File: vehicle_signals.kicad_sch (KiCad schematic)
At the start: 24 parts, among them IC4 TLIN1027DRQ1, U10 LTV-827S, U11 LTV-827S, U12 LTV-827S, U13 LTV-827S

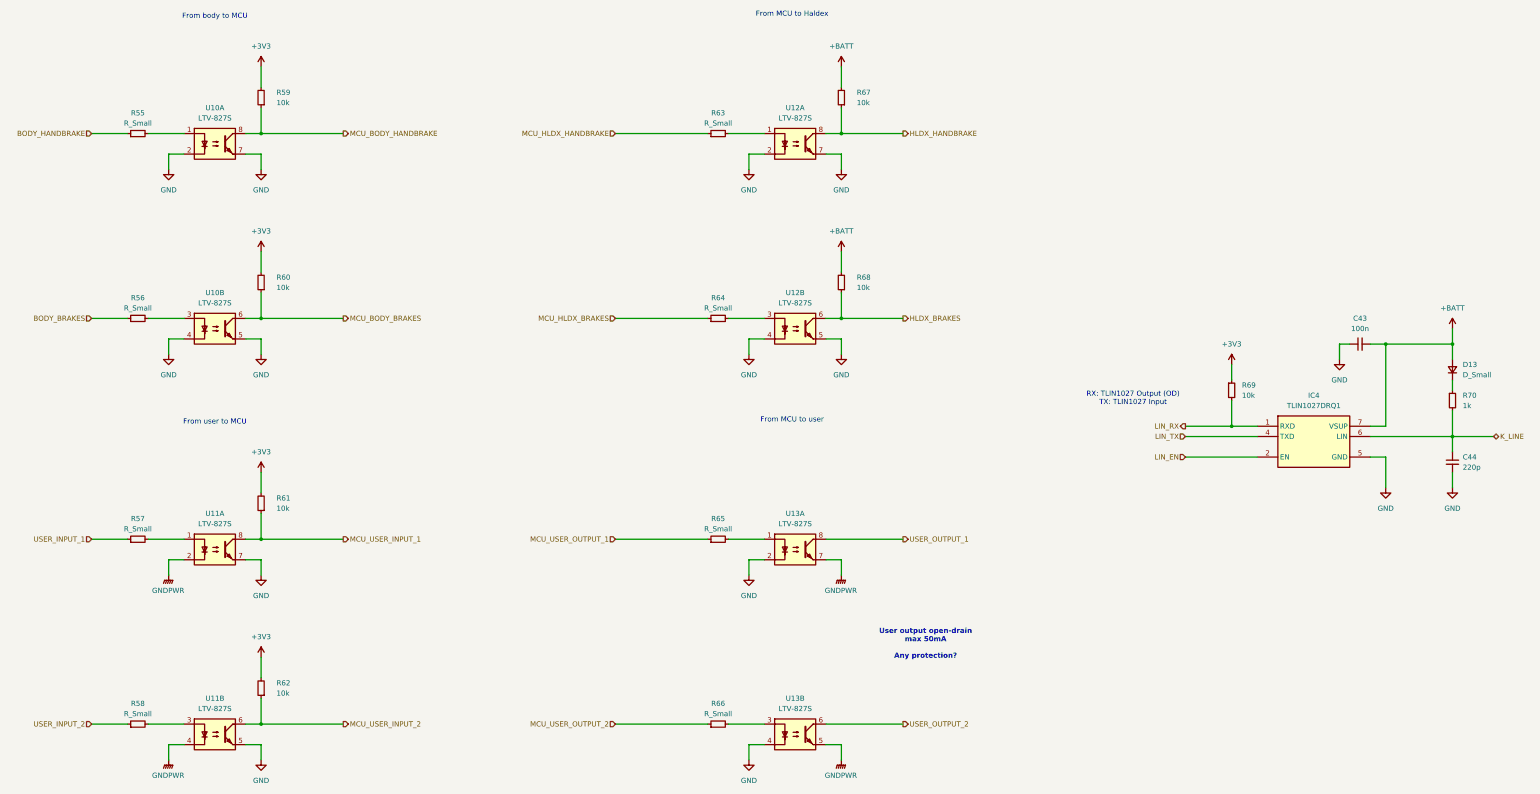
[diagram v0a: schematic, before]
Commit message: vehicle signals: using solid state relais
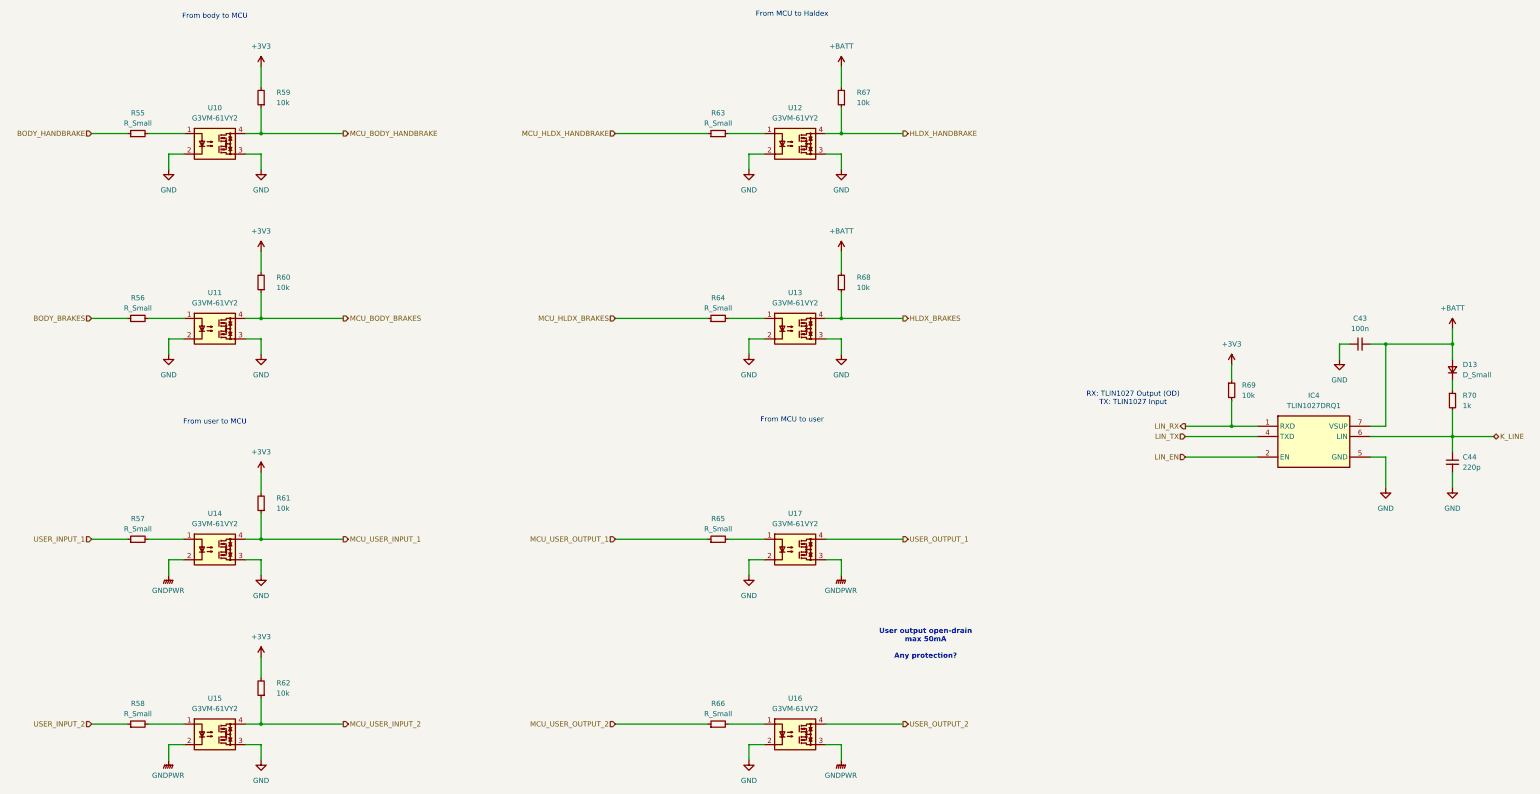
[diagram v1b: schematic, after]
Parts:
- removed U10, U11, U12, U13: LTV-827S, Package_DIP:SMDIP-8_W9.53mm, symbol Isolator:LTV-827S
- added U10, U11, U12, U13, U14, U15, U16, U17: G3VM-61VY2, symbol G3VM-61VY2:G3VM-61VY2
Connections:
- net GND: now also U10.2, U10.3, U11.2, U11.3, U12.2, U12.3, U13.2, U13.3, U14.3, U15.3, U16.2, U17.2
- net GNDPWR: now also U14.2, U15.2, U16.3, U17.3
- net HLDX_BRAKES: now also U13.4
- net HLDX_HANDBRAKE: now also U12.4
- net MCU_BODY_BRAKES: now also U11.4
- net MCU_BODY_HANDBRAKE: now also U10.4
- net MCU_USER_INPUT_1: now also U14.4
- net MCU_USER_INPUT_2: now also U15.4
- net USER_OUTPUT_1: now also U17.4
- net USER_OUTPUT_2: now also U16.4
- net at R63.2: now also U12.1
- net at R66.2: now also U16.1
- net at R65.2: now also U17.1
- net at R55.2: now also U10.1
- net at R56.2: now also U11.1
- net at R57.2: now also U14.1
- net at R58.2: now also U15.1
- net at R64.2: now also U13.1

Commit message: sch: fixing component footprints
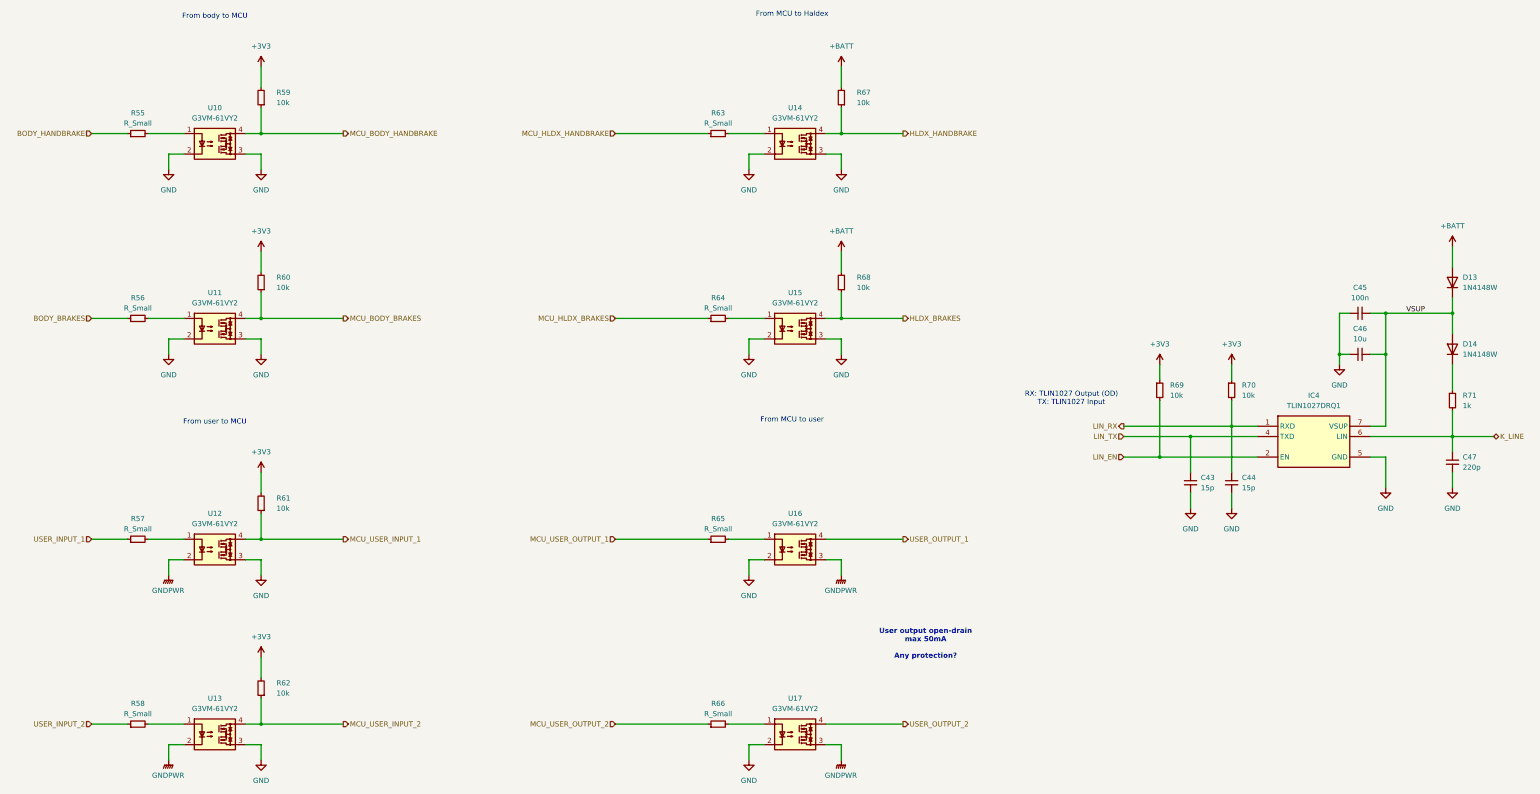
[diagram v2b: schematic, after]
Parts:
- removed D13: D_Small, symbol Device:D_Small
- added C43, C44: 15p, Capacitor_SMD:C_0603_1608Metric_Pad1.08x0.95mm_HandSolder, symbol Device:C_Small
- added C46: 10u, Capacitor_SMD:C_0603_1608Metric_Pad1.08x0.95mm_HandSolder, symbol Device:C_Small
- added D13, D14: 1N4148W, Diode_SMD:D_SOD-123, symbol Diode:1N4148W
- added R69: 10k, Resistor_SMD:R_0603_1608Metric_Pad0.98x0.95mm_HandSolder, symbol Device:R_Small
- IC4: footprint SOIC127P600X175-8N -> TLIN1027DRQ1:SOIC127P600X175-8N
- R71: renamed from R70; footprint Resistor_SMD:R_0603_1608Metric_Pad0.98x0.95mm_HandSolder -> Resistor_SMD:R_1206_3216Metric_Pad1.30x1.75mm_HandSolder
- U10, U11: footprint (none) -> G3VM-61VY2:SOP254P700X230-4N
- U12: renamed from U14; footprint (none) -> G3VM-61VY2:SOP254P700X230-4N
- U13: renamed from U15; footprint (none) -> G3VM-61VY2:SOP254P700X230-4N
- U14: renamed from U12; footprint (none) -> G3VM-61VY2:SOP254P700X230-4N
- U15: renamed from U13; footprint (none) -> G3VM-61VY2:SOP254P700X230-4N
- U16: renamed from U17; footprint (none) -> G3VM-61VY2:SOP254P700X230-4N
- U17: renamed from U16; footprint (none) -> G3VM-61VY2:SOP254P700X230-4N
- renumbered C43 to C45, C44 to C47, R69 to R70
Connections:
- net +3V3: now also R69.1
- net +BATT: now also D13.2 (A); no longer C45.2, IC4.7 (VSUP)
- net GND: now also C43.2, C44.2, C46.1
- net LIN_EN: now also R69.2
- net LIN_RX: now also C44.1
- net LIN_TX: now also C43.1
- net at R71.1: now also D14.1 (K)
- new net VSUP: C45.2, C46.2, D13.1 (K), D14.2 (A), IC4.7 (VSUP)
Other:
- moved on the sheet: C45

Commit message: brd: routing in progress
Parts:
- added C51: 100n, Capacitor_SMD:C_0603_1608Metric_Pad1.08x0.95mm_HandSolder, symbol Device:C_Small
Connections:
- net GND: now also C51.1
- net VSUP: now also C51.2
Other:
- moved on the sheet: C45, C46, D13, D14
